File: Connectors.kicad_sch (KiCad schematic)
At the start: 25 parts, among them J1 TC2070-IDC-FP (DNP), J201 JST-PH, J203 Serial Interface, J204 Micro_SD_Card_Det2, J206 USB_C_Receptacle_USB2.0, J7 EPD_Conn, J7 LORA_Conn, U201 USBLC6-2SC6

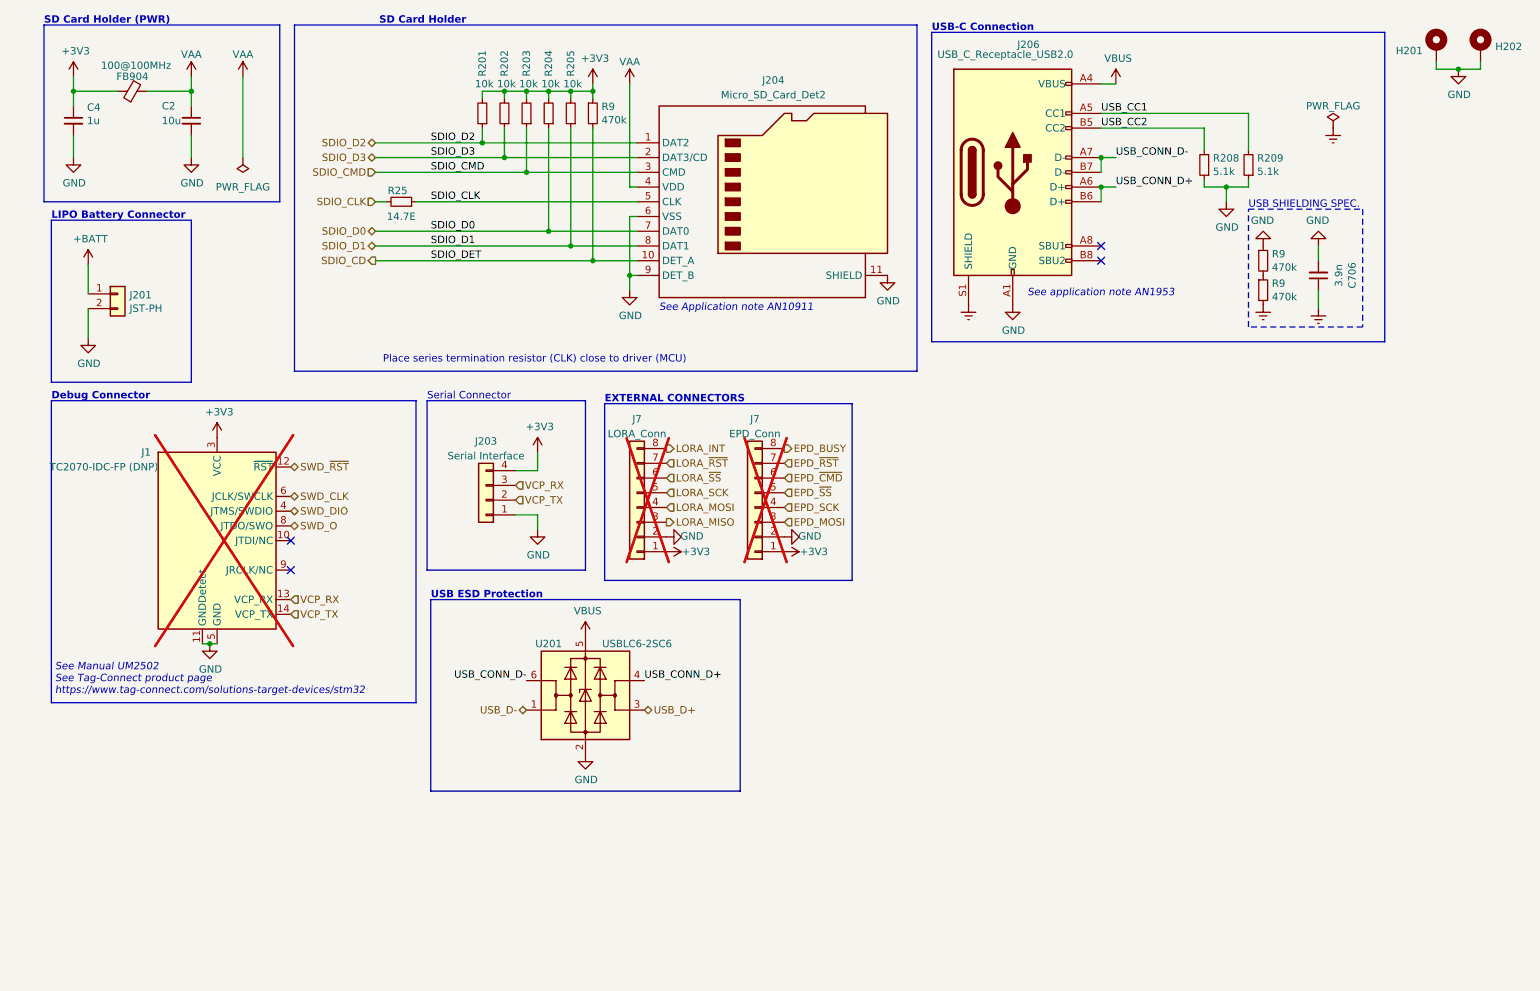
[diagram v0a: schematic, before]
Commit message: (sch) add SDIO bus spec
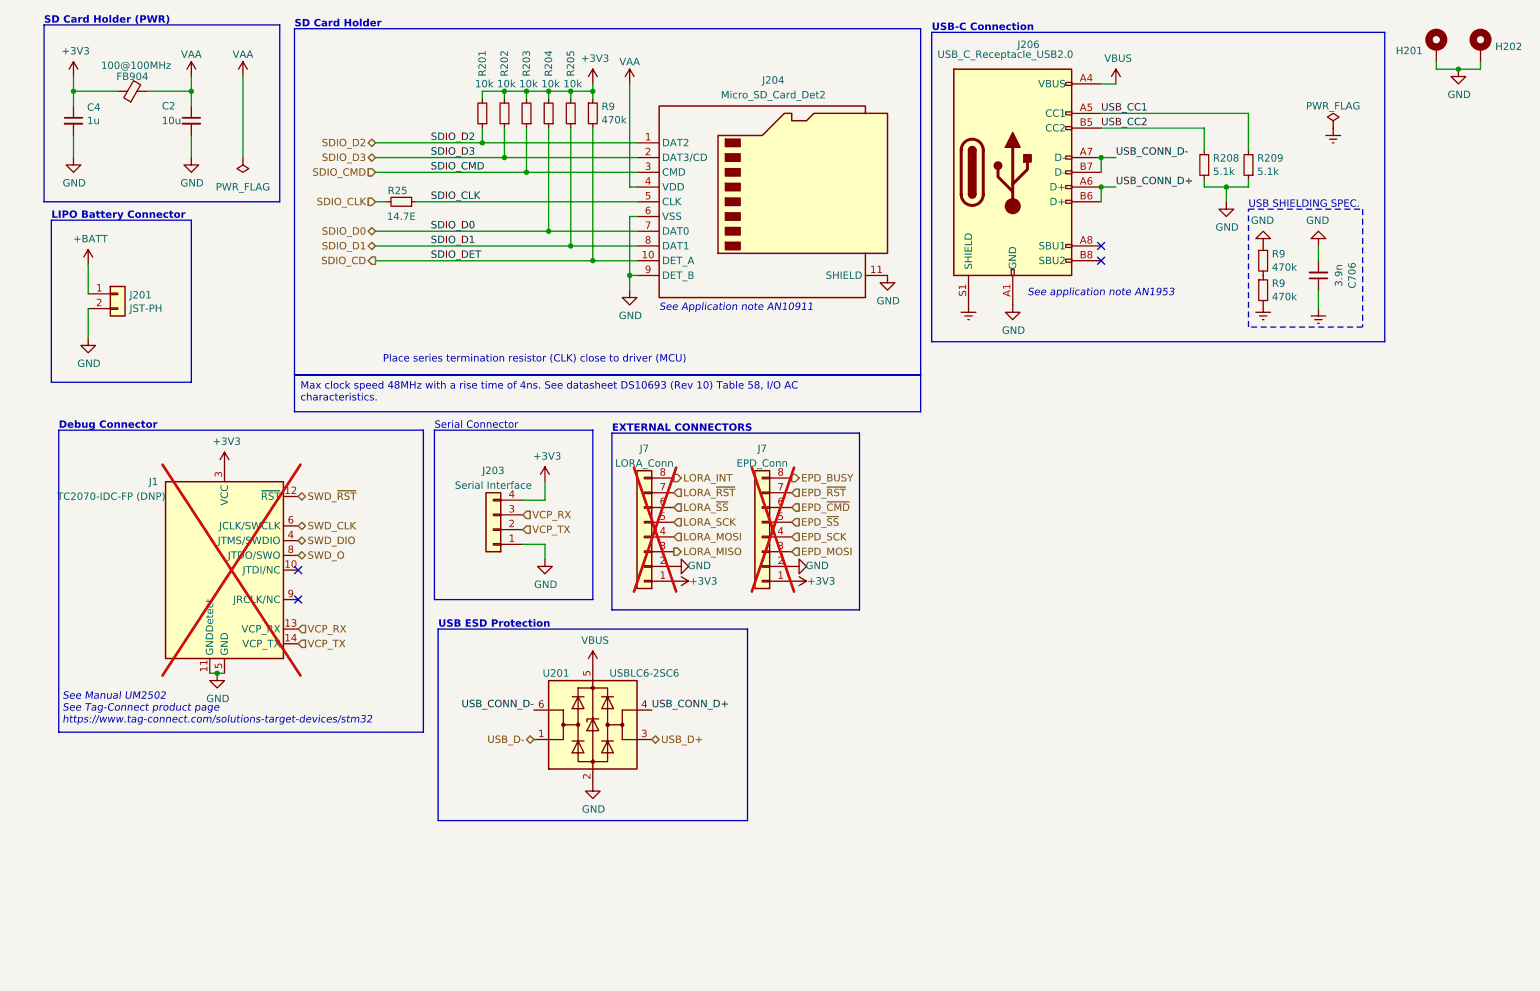
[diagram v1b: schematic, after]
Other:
- moved on the sheet: J1, J203, J7, U201

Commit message: change 10u cap from 0805 to 0402
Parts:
- C2: footprint Capacitor_SMD:C_0805_2012Metric_Pad1.18x1.45mm_HandSolder -> Capacitor_SMD:C_0402_1005Metric; MPN C0805C106K9PACTU -> GRM155R60J106ME05D; Mfr. KEMET -> Murata
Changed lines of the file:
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@@
       (effects (font (size 1.27 1.27)) (justify left))
     )
-    (property "Footprint" "Capacitor_SMD:C_0805_2012Metric_Pad1.18x1.45mm_HandSolder" (at 39.37 31.115 0)
+    (property "Footprint" "Capacitor_SMD:C_0402_1005Metric" (at 39.37 31.115 0)
       (effects (font (size 1.27 1.27)) hide)
     )
@@
       (effects (font (size 1.27 1.27)) hide)
     )
-    (property "MPN" "C0805C106K9PACTU" (at 39.37 31.115 0)
+    (property "MPN" "GRM155R60J106ME05D" (at 39.37 31.115 0)
       (effects (font (size 1.27 1.27)) hide)
     )
-    (property "Mfr." "KEMET" (at 39.37 31.115 0)
+    (property "Mfr." "Murata" (at 39.37 31.115 0)
       (effects (font (size 1.27 1.27)) hide)
     )

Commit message: replace passives with 0402
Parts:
- C4: footprint Capacitor_SMD:C_0603_1608Metric_Pad1.08x0.95mm_HandSolder -> Capacitor_SMD:C_0402_1005Metric; MPN C0603C105K8RACTU -> C0402C105K9PACTU
- FB904: footprint Inductor_SMD:L_0603_1608Metric_Pad1.05x0.95mm_HandSolder -> Inductor_SMD:L_0402_1005Metric; MPN BLM18KG101TZ1D -> BLM15HD102SN1D
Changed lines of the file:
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@@
       (effects (font (size 1.27 1.27)))
     )
-    (property "Footprint" "Inductor_SMD:L_0603_1608Metric_Pad1.05x0.95mm_HandSolder" (at 29.21 27.813 90)
+    (property "Footprint" "Inductor_SMD:L_0402_1005Metric" (at 29.21 27.813 90)
       (effects (font (size 1.27 1.27)) hide)
     )
@@
       (effects (font (size 1.27 1.27)) hide)
     )
-    (property "MPN" "BLM18KG101TZ1D" (at 29.21 26.035 90)
+    (property "MPN" "BLM15HD102SN1D" (at 29.21 26.035 90)
       (effects (font (size 1.27 1.27)) hide)
     )
@@
       (effects (font (size 1.27 1.27)) (justify left))
     )
-    (property "Footprint" "Capacitor_SMD:C_0603_1608Metric_Pad1.08x0.95mm_HandSolder" (at 19.05 31.115 0)
+    (property "Footprint" "Capacitor_SMD:C_0402_1005Metric" (at 19.05 31.115 0)
       (effects (font (size 1.27 1.27)) hide)
     )
@@
       (effects (font (size 1.27 1.27)) (justify left) hide)
     )
-    (property "MPN" "C0603C105K8RACTU" (at 19.05 31.115 0)
+    (property "MPN" "C0402C105K9PACTU" (at 19.05 31.115 0)
       (effects (font (size 1.27 1.27)) hide)
     )

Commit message: (sch) DNP VCP LED Res.
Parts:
- J203: now not fitted; now left out of the parts list
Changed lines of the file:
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@@
   )
   (symbol (lib_id "Connector_Generic:Conn_01x04") (at 91.44 101.6 180) (unit 1)
-    (in_bom yes) (on_board yes) (dnp no) (fields_autoplaced)
+    (in_bom no) (on_board yes) (dnp yes) (fields_autoplaced)
     (property "Reference" "J203" (at 91.44 91.44 0)
       (effects (font (size 1.27 1.27)))
@@
       (effects (font (size 1.27 1.27)) hide)
     )
+    (property "MPN" "" (at 91.44 101.6 0)
+      (effects (font (size 1.27 1.27)) hide)
+    )
+    (property "Mfr." "" (at 91.44 101.6 0)
+      (effects (font (size 1.27 1.27)) hide)
+    )

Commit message: (pcb) route power
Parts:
- added C2 (x2): 10u, Capacitor_SMD:C_0402_1005Metric, symbol Device:C_Small
- added C4: 1u, Capacitor_SMD:C_0402_1005Metric, symbol Device:C_Small
- added CB1: 100n, Capacitor_SMD:C_0402_1005Metric, symbol Device:C_Small
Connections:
- net +3V3: now also C2.1, C2.1, C4.1, CB1.1
- net GND: now also C2.2, C2.2, C4.2, CB1.2
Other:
- moved on the sheet: C706, H201, H202, J206, R208, R209, R9

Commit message: (sch) fix SDIO_CLK net label
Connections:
- net SDIO_CLK: no longer J204.5 (CLK), R25.1
- new net SDIO_CLK_TERM: J204.5 (CLK), R25.1
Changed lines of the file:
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@@
     (effects (font (size 1.27 1.27)) (justify right bottom))
   )
-  (label "SDIO_CLK" (at 80.645 45.085 0) (fields_autoplaced)
+  (label "SDIO_CLK_TERM" (at 80.645 45.085 0) (fields_autoplaced)
     (effects (font (size 1.27 1.27)) (justify left bottom))
   )

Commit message: (sch) run DRC
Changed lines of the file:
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@@
-    (effects (font (size 1.27 1.27)) (justify left bottom))
-  )
-  (label "SDIO_DET" (at 80.645 55.245 0) (fields_autoplaced)
     (effects (font (size 1.27 1.27)) (justify left bottom))
   )

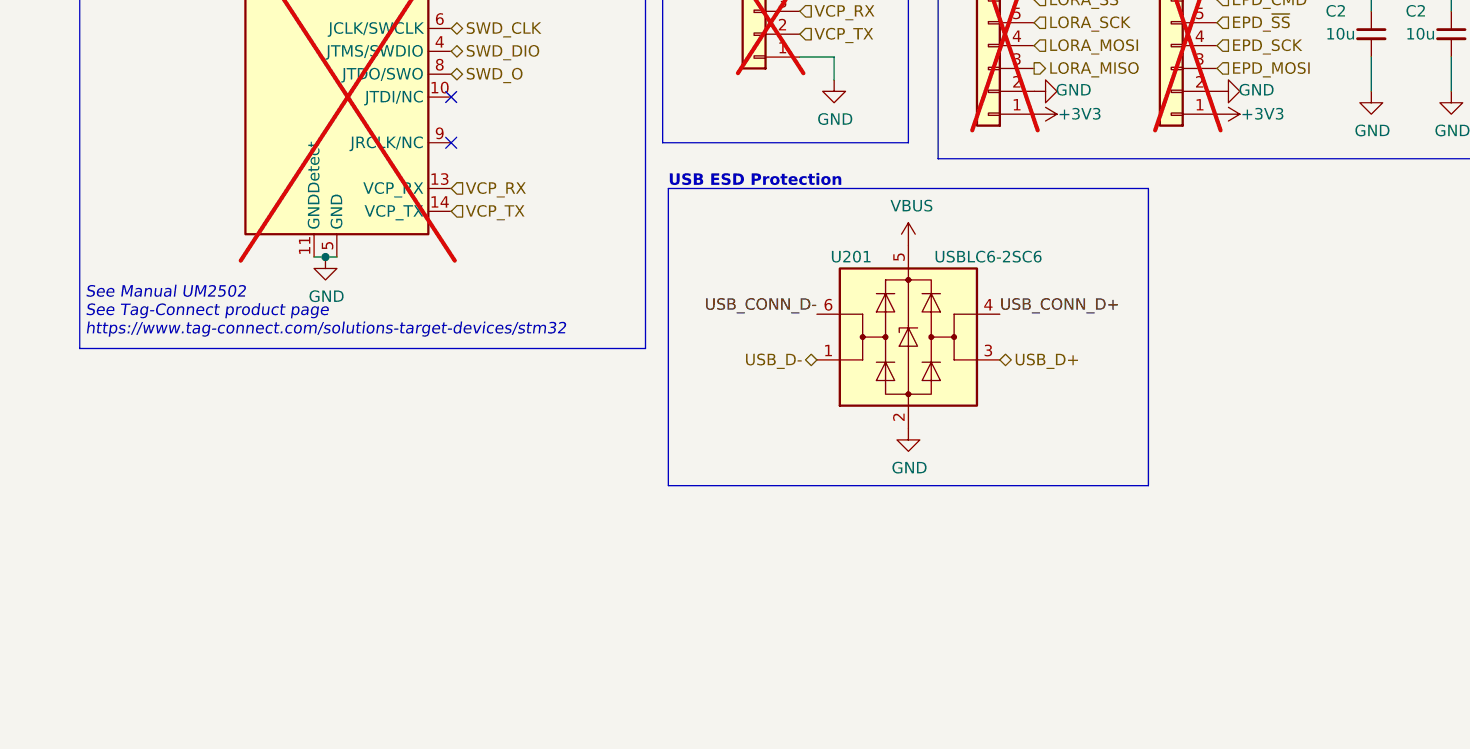
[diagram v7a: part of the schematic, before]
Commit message: (sch) consoldate BOM
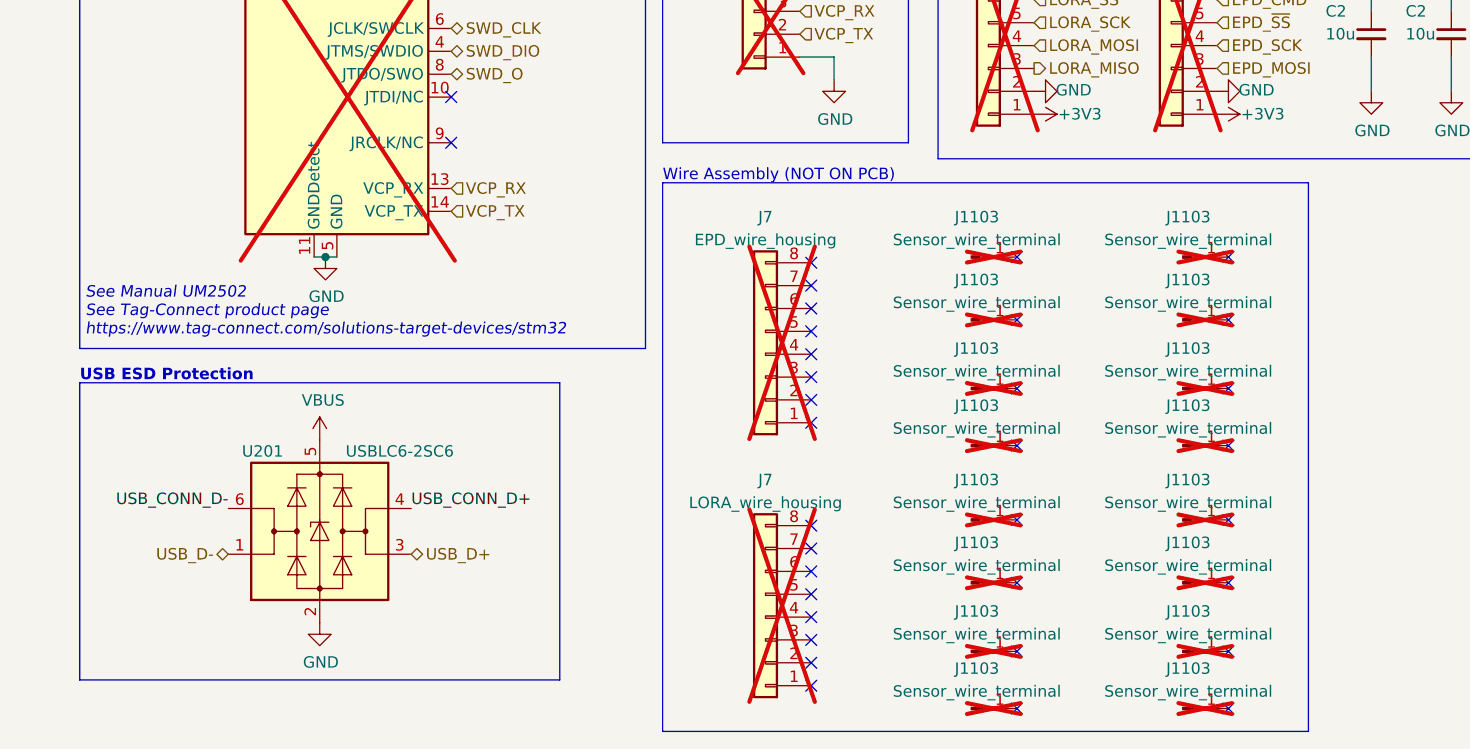
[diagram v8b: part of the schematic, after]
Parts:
- added J1103 (x16): Sensor_wire_terminal, symbol Connector:Conn_01x01_Pin
- added J7: EPD_wire_housing, symbol Connector_Generic:Conn_01x08
- added J7: LORA_wire_housing, symbol Connector_Generic:Conn_01x08
- J1: Mfr. Samtec -> Tag Connect
- J7: MPN (none) -> 10114828-11108LF; Mfr. (none) -> Amphenol
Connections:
- no-connect marks 4 -> 36
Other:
- note added: "Wire Assembly (NOT ON PCB)"
- moved on the sheet: U201
